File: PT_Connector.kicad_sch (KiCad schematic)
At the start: 14 parts, among them J1 Conn_01x03_Pin, J10 Conn_01x03_Pin, J11 DSUB_15pin/VGA Veritical Fema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, J12 Conn_01x03_Pin, J2 DSUB_15pin/VGA Veritical Fema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, J22 DSUB_15pin/VGA Veritical Fema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, J23 Conn_01x03_Pin, J24 DSUB_15pin/VGA Veritical Fema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, J3 Conn_01x03_Pin, J4 DSUB_15pin/VGA Veritical Fema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

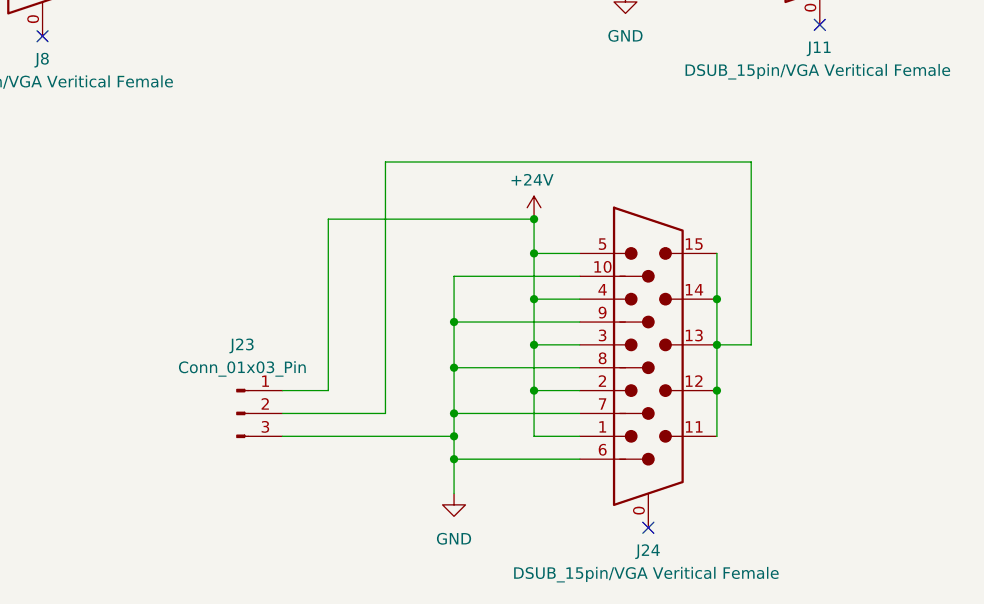
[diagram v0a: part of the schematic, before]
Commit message: grounded mounting holes
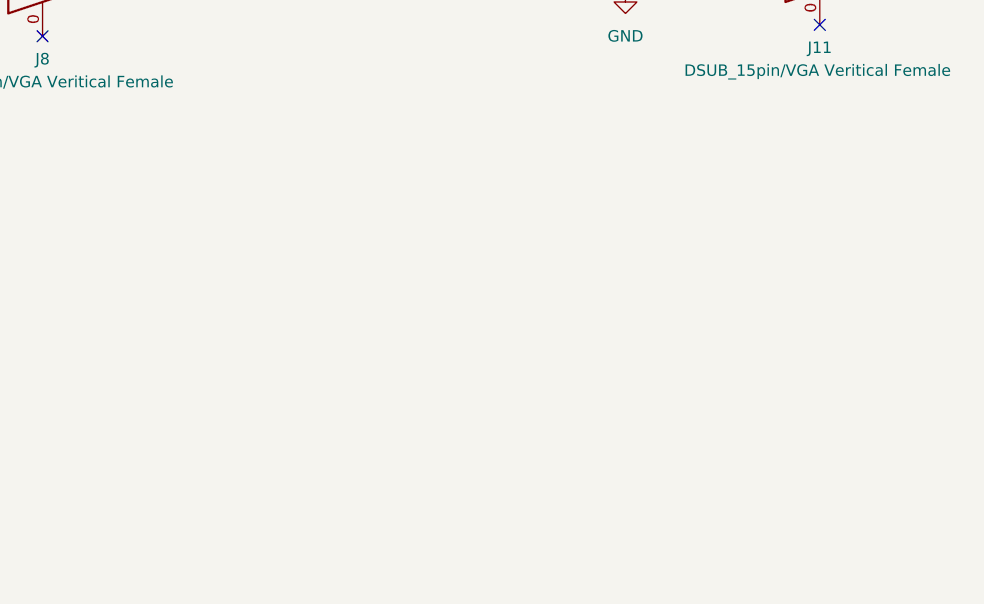
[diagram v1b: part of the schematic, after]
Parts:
- removed J23: Conn_01x03_Pin, Connector_PinHeader_2.54mm:PinHeader_1x03_P2.54mm_Vertical, symbol Connector:Conn_01x03_Pin
- removed J24: DSUB_15pin/VGA Veritical Female, UCIRP-KiCAD-Lib:Connector_VGA_Vertical, symbol UCIRP-KiCAD-Lib:Connector_VGA_vertical
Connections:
- no-connect marks 7 -> 6

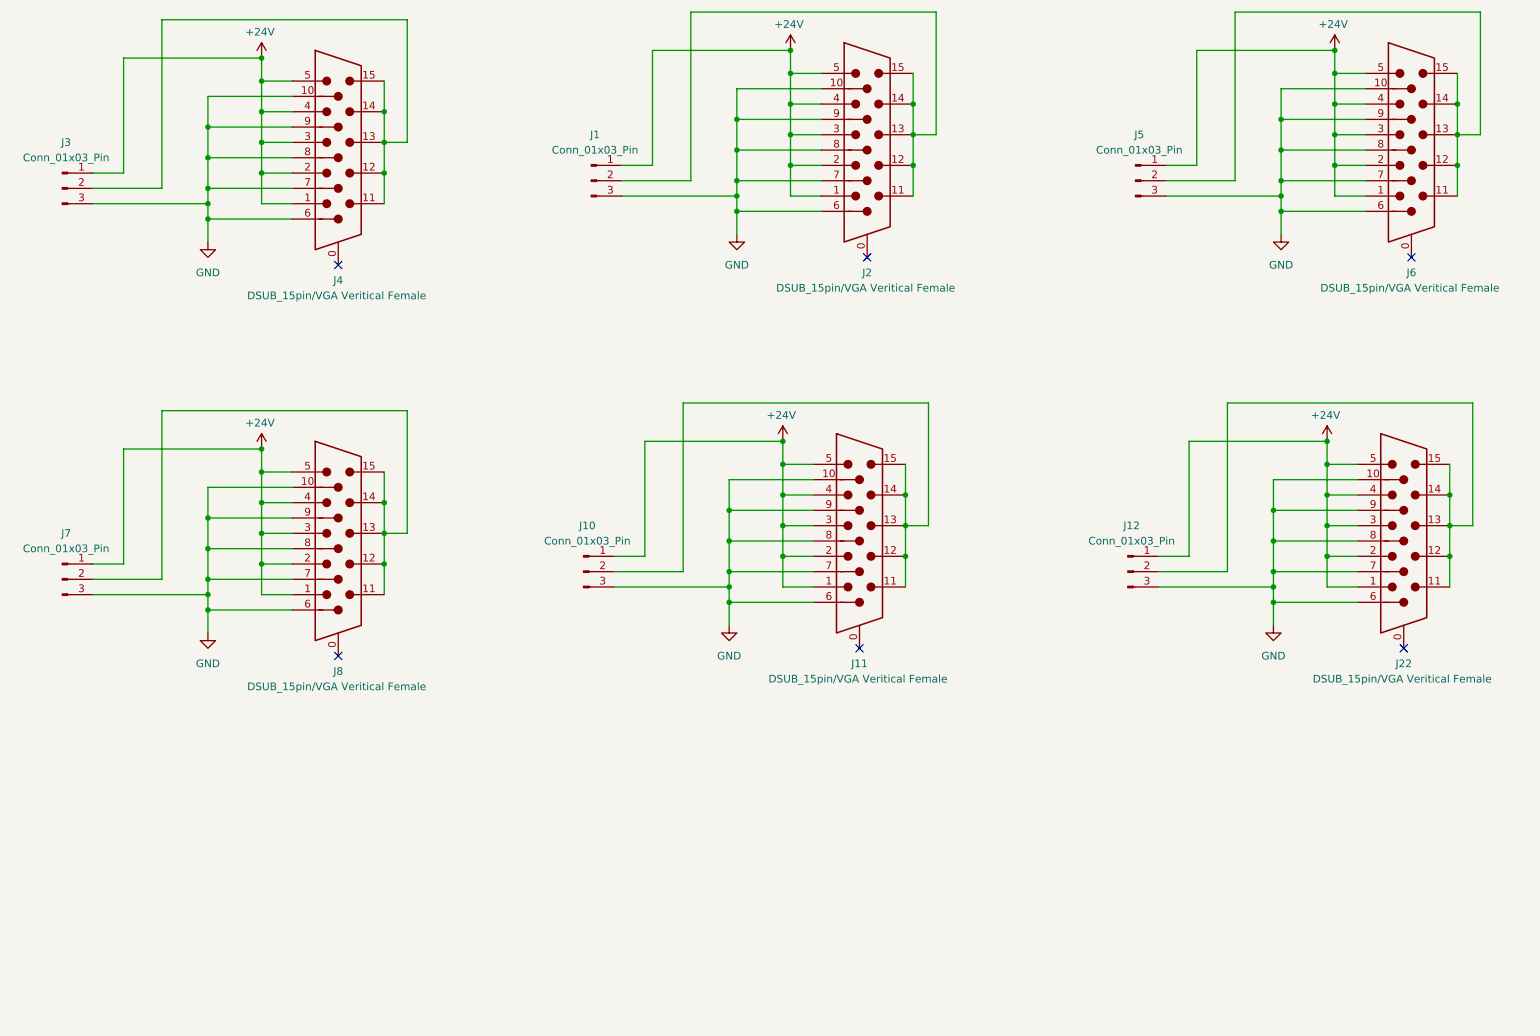
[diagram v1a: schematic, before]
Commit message: silkscreen labeling, fixed trace thicknesses
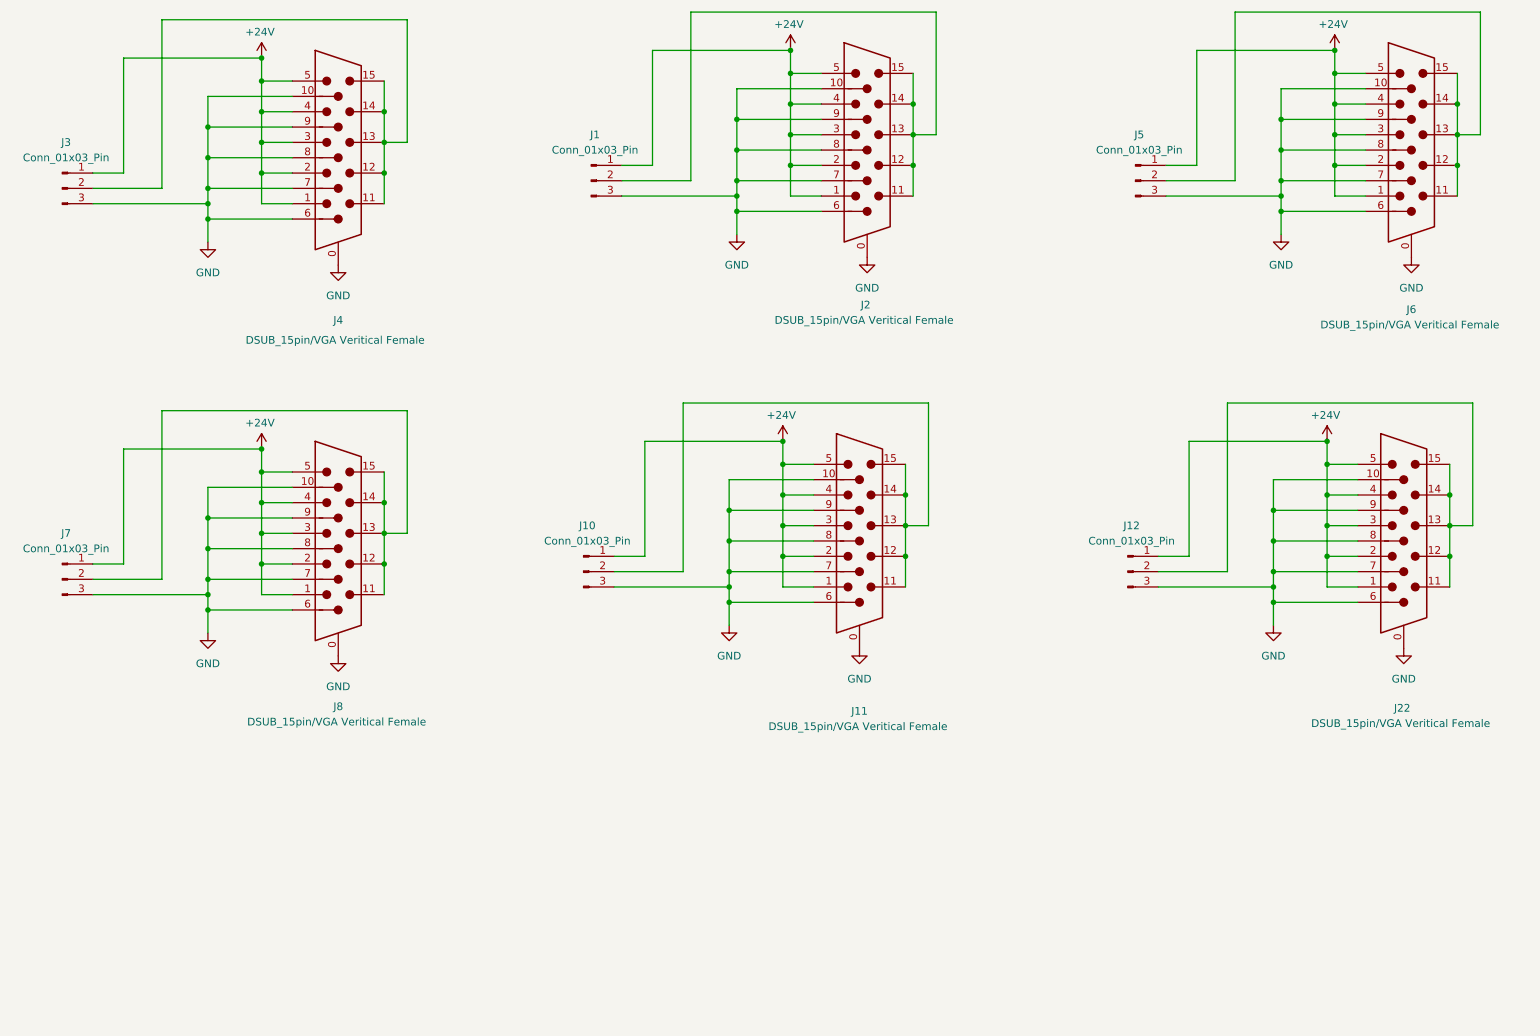
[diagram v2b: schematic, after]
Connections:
- net GND: now also J11.0, J2.0, J22.0, J4.0, J6.0, J8.0
- no-connect marks 6 -> 0

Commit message: grounded pin 11 on PT Connectors
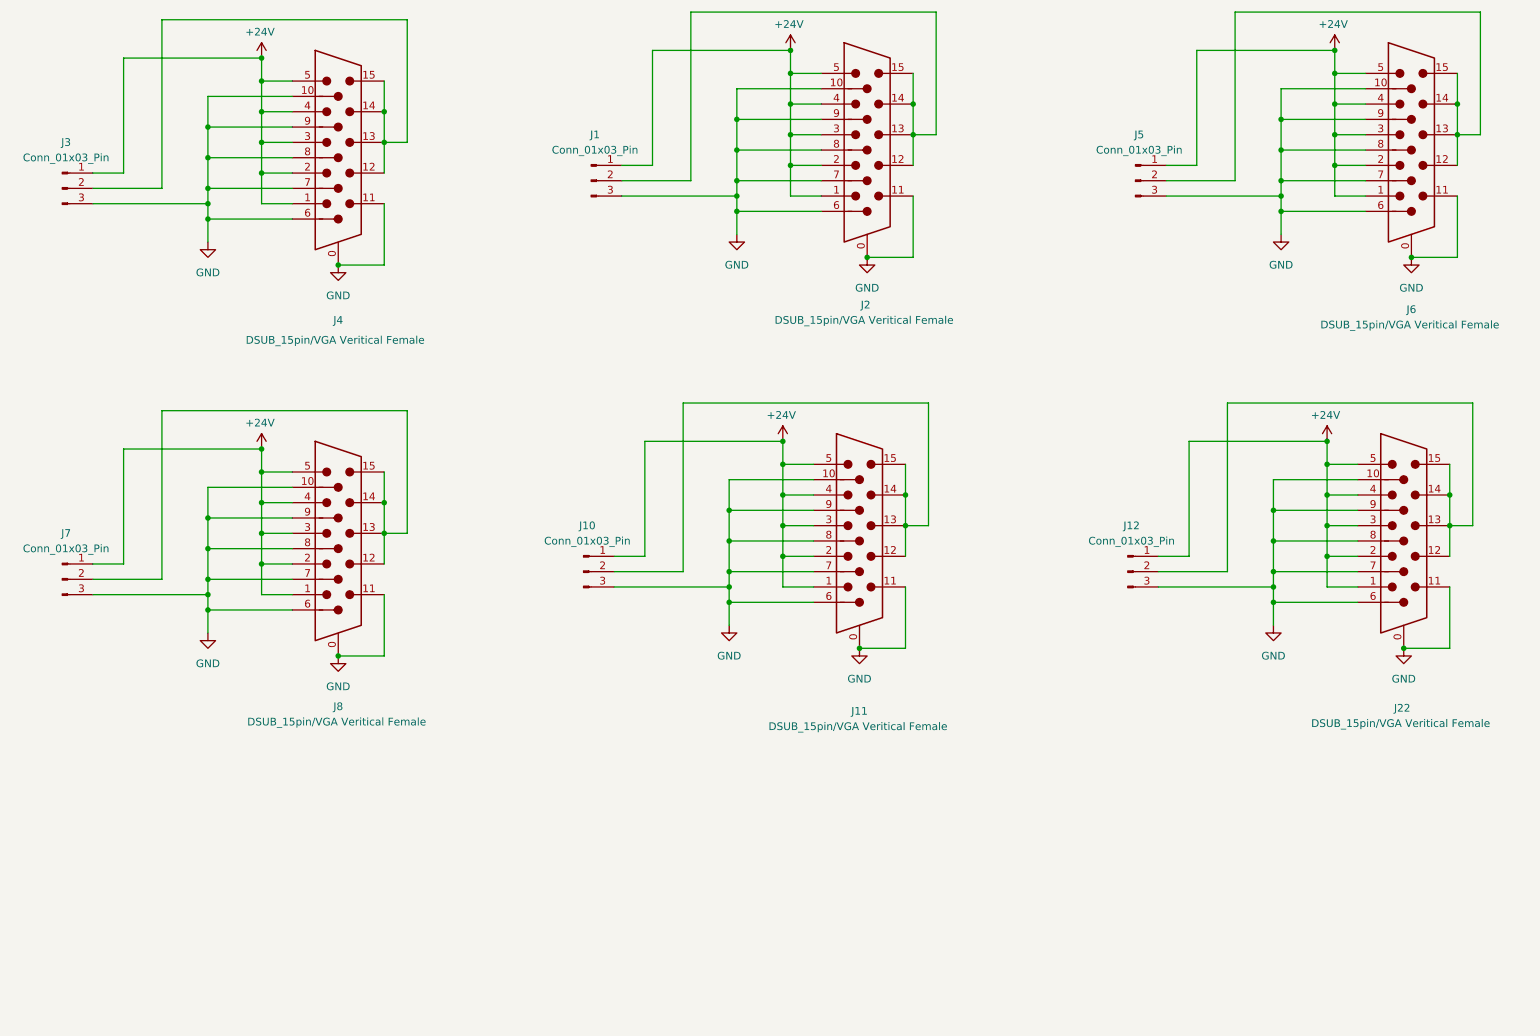
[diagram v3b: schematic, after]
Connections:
- net GND: now also J11.11, J2.11, J22.11, J4.11, J6.11, J8.11
- net at J12.2 (Pin_2), J22.12, J22.13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: no longer J22.11
- net at J7.2 (Pin_2), J8.12, J8.13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: no longer J8.11
- net at J1.2 (Pin_2), J2.12, J2.13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: no longer J2.11
- net at J3.2 (Pin_2), J4.12, J4.13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: no longer J4.11
- net at J5.2 (Pin_2), J6.12, J6.13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: no longer J6.11
- net at J10.2 (Pin_2), J11.12, J11.13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: no longer J11.11
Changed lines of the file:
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@@
 	(paper "A4")
 	(junction
-		(at 172.72 49.53)
-		(diameter 0)
-		(color 0 0 0 0)
-	)
-	(junction
 		(at 143.51 57.15)
 		(diameter 0)
@@
 	)
 	(junction
-		(at 262.89 49.53)
-		(diameter 0)
-		(color 0 0 0 0)
-	)
-	(junction
 		(at 85.09 110.49)
 		(diameter 0)
@@
 	)
 	(junction
+		(at 163.83 129.54)
+		(diameter 0)
+		(color 0 0 0 0)
+	)
+	(junction
 		(at 55.88 55.88)
 		(diameter 0)
@@
 	)
 	(junction
+		(at 77.47 130.81)
+		(diameter 0)
+		(color 0 0 0 0)
+	)
+	(junction
 		(at 242.57 30.48)
 		(diameter 0)
@@
 	)
 	(junction
-		(at 85.09 115.57)
-		(diameter 0)
-		(color 0 0 0 0)
-	)
-	(junction
-		(at 171.45 114.3)
+		(at 77.47 66.04)
 		(diameter 0)
 		(color 0 0 0 0)
@@
 	)
 	(junction
+		(at 165.1 64.77)
+		(diameter 0)
+		(color 0 0 0 0)
+	)
+	(junction
 		(at 232.41 119.38)
 		(diameter 0)
@@
 	)
 	(junction
-		(at 261.62 114.3)
-		(diameter 0)
-		(color 0 0 0 0)
-	)
-	(junction
 		(at 64.77 50.8)
 		(diameter 0)
@@
 	)
 	(junction
+		(at 255.27 64.77)
+		(diameter 0)
+		(color 0 0 0 0)
+	)
+	(junction
 		(at 142.24 121.92)
 		(diameter 0)
@@
 	)
 	(junction
-		(at 85.09 50.8)
-		(diameter 0)
-		(color 0 0 0 0)
-	)
-	(junction
 		(at 55.88 118.11)
 		(diameter 0)
@@
 	)
 	(junction
+		(at 254 129.54)
+		(diameter 0)
+		(color 0 0 0 0)
+	)
+	(junction
 		(at 85.09 105.41)
 		(diameter 0)
@@
 	(wire
 		(pts
+			(xy 254 129.54) (xy 261.62 129.54)
+		)
+		(stroke
+			(width 0)
+			(type default)
+		)
+	)
+	(wire
+		(pts
 			(xy 55.88 113.03) (xy 55.88 118.11)
 		)
@@
 	(wire
 		(pts
-			(xy 262.89 49.53) (xy 262.89 54.61)
-		)
-		(stroke
-			(width 0)
-			(type default)
-		)
-	)
-	(wire
-		(pts
 			(xy 134.62 88.9) (xy 134.62 116.84)
 		)
@@
 	(wire
 		(pts
+			(xy 85.09 55.88) (xy 85.09 66.04)
+		)
+		(stroke
+			(width 0)
+			(type default)
+		)
+	)
+	(wire
+		(pts
 			(xy 226.06 24.13) (xy 226.06 52.07)
 		)
@@
 	(wire
 		(pts
-			(xy 172.72 49.53) (xy 172.72 54.61)
+			(xy 85.09 120.65) (xy 85.09 130.81)
 		)
 		(stroke
@@
 	(wire
 		(pts
+			(xy 77.47 130.81) (xy 85.09 130.81)
+		)
+		(stroke
+			(width 0)
+			(type default)
+		)
+	)
+	(wire
+		(pts
 			(xy 152.4 39.37) (xy 157.48 39.37)
 		)
@@
 	(wire
 		(pts
+			(xy 165.1 64.77) (xy 172.72 64.77)
+		)
+		(stroke
+			(width 0)
+			(type default)
+		)
+	)
+	(wire
+		(pts
 			(xy 233.68 57.15) (xy 247.65 57.15)
 		)
@@
 	(wire
 		(pts
-			(xy 85.09 50.8) (xy 85.09 55.88)
-		)
-		(stroke
-			(width 0)
-			(type default)
-		)
-	)
-	(wire
-		(pts
 			(xy 88.9 110.49) (xy 88.9 90.17)
 		)
@@
 	(wire
 		(pts
+			(xy 163.83 129.54) (xy 171.45 129.54)
+		)
+		(stroke
+			(width 0)
+			(type default)
+		)
+	)
+	(wire
+		(pts
 			(xy 143.51 41.91) (xy 157.48 41.91)
 		)
@@
 	(wire
 		(pts
-			(xy 85.09 115.57) (xy 85.09 120.65)
-		)
-		(stroke
-			(width 0)
-			(type default)
-		)
-	)
-	(wire
-		(pts
 			(xy 242.57 39.37) (xy 242.57 44.45)
 		)
@@
 	(wire
 		(pts
+			(xy 171.45 119.38) (xy 171.45 129.54)
+		)
+		(stroke
+			(width 0)
+			(type default)
+		)
+	)
+	(wire
+		(pts
 			(xy 64.77 45.72) (xy 69.85 45.72)
 		)
@@
 	(wire
 		(pts
-			(xy 171.45 114.3) (xy 171.45 119.38)
-		)
-		(stroke
-			(width 0)
-			(type default)
-		)
-	)
-	(wire
-		(pts
 			(xy 151.13 114.3) (xy 156.21 114.3)
 		)
@@
 	(wire
 		(pts
+			(xy 255.27 64.77) (xy 262.89 64.77)
+		)
+		(stroke
+			(width 0)
+			(type default)
+		)
+	)
+	(wire
+		(pts
+			(xy 77.47 66.04) (xy 85.09 66.04)
+		)
+		(stroke
+			(width 0)
+			(type default)
+		)
+	)
+	(wire
+		(pts
 			(xy 219.71 30.48) (xy 242.57 30.48)
 		)
@@
 	(wire
 		(pts
+			(xy 172.72 54.61) (xy 172.72 64.77)
+		)
+		(stroke
+			(width 0)
+			(type default)
+		)
+	)
+	(wire
+		(pts
 			(xy 176.53 24.13) (xy 135.89 24.13)
 		)
@@
 	(wire
 		(pts
-			(xy 261.62 114.3) (xy 261.62 119.38)
-		)
-		(stroke
-			(width 0)
-			(type default)
-		)
-	)
-	(wire
-		(pts
 			(xy 36.83 53.34) (xy 48.26 53.34)
 		)
@@
 	(wire
 		(pts
+			(xy 261.62 119.38) (xy 261.62 129.54)
+		)
+		(stroke
+			(width 0)
+			(type default)
+		)
+	)
+	(wire
+		(pts
 			(xy 88.9 25.4) (xy 48.26 25.4)
 		)
@@
 		)
 		(stroke
+			(width 0)
+			(type default)
+		)
+	)
+	(wire
+		(pts
+			(xy 262.89 54.61) (xy 262.89 64.77)
+		)
+		(stroke
